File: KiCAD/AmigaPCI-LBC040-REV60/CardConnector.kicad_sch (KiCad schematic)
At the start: 42 parts, among them CN100 DIN41612_03x50, CN111 SPI, U111 ICE40HX4K-TQ144, U409F2 W25X20CLSN, X100 80MHz

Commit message: Add JLCPCB part numbers to KiCAD schematic.
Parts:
- C113, C114, C115, C116, C117, C135, C138: LCSC (none) -> C88724
- C122, C123, C124, C125, C126, C127, C128, C129, C130, C131, C133, C136, C137: LCSC (none) -> C14663
- C132, C134: LCSC (none) -> C96446
- CN111: LCSC (none) -> C37208
- R106, R107: LCSC (none) -> C25804
- R108, R109: LCSC (none) -> C22775
- R112, R113, R114, R115, R116, R117, R118, R119, R120: LCSC (none) -> C23345
- U111: LCSC (none) -> C1521989
- U409F2: LCSC (none) -> C34591
- X100: LCSC (none) -> C17234777

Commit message: Change JLCPCB part number for 80MHz oscillator.
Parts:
- X100: LCSC C17234777 -> C557215
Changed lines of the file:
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@@
 			)
 		)
-		(property "LCSC" "C17234777"
+		(property "LCSC" "C557215"
 			(at 358.14 157.48 0)
 			(effects

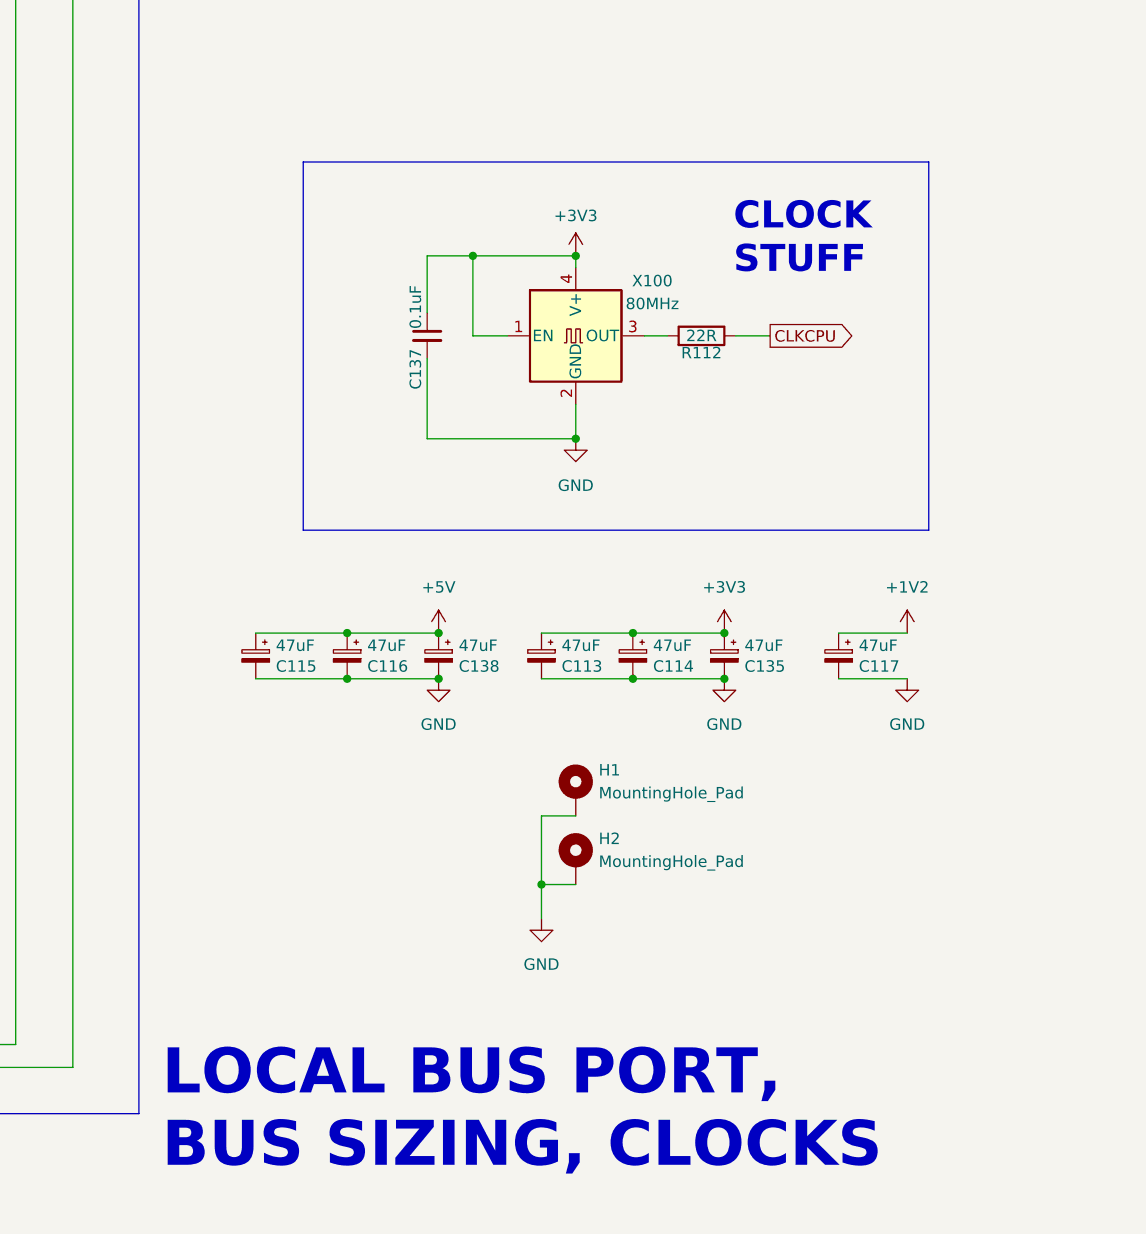
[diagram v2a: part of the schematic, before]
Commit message: Add part number for DIN41612 connector.
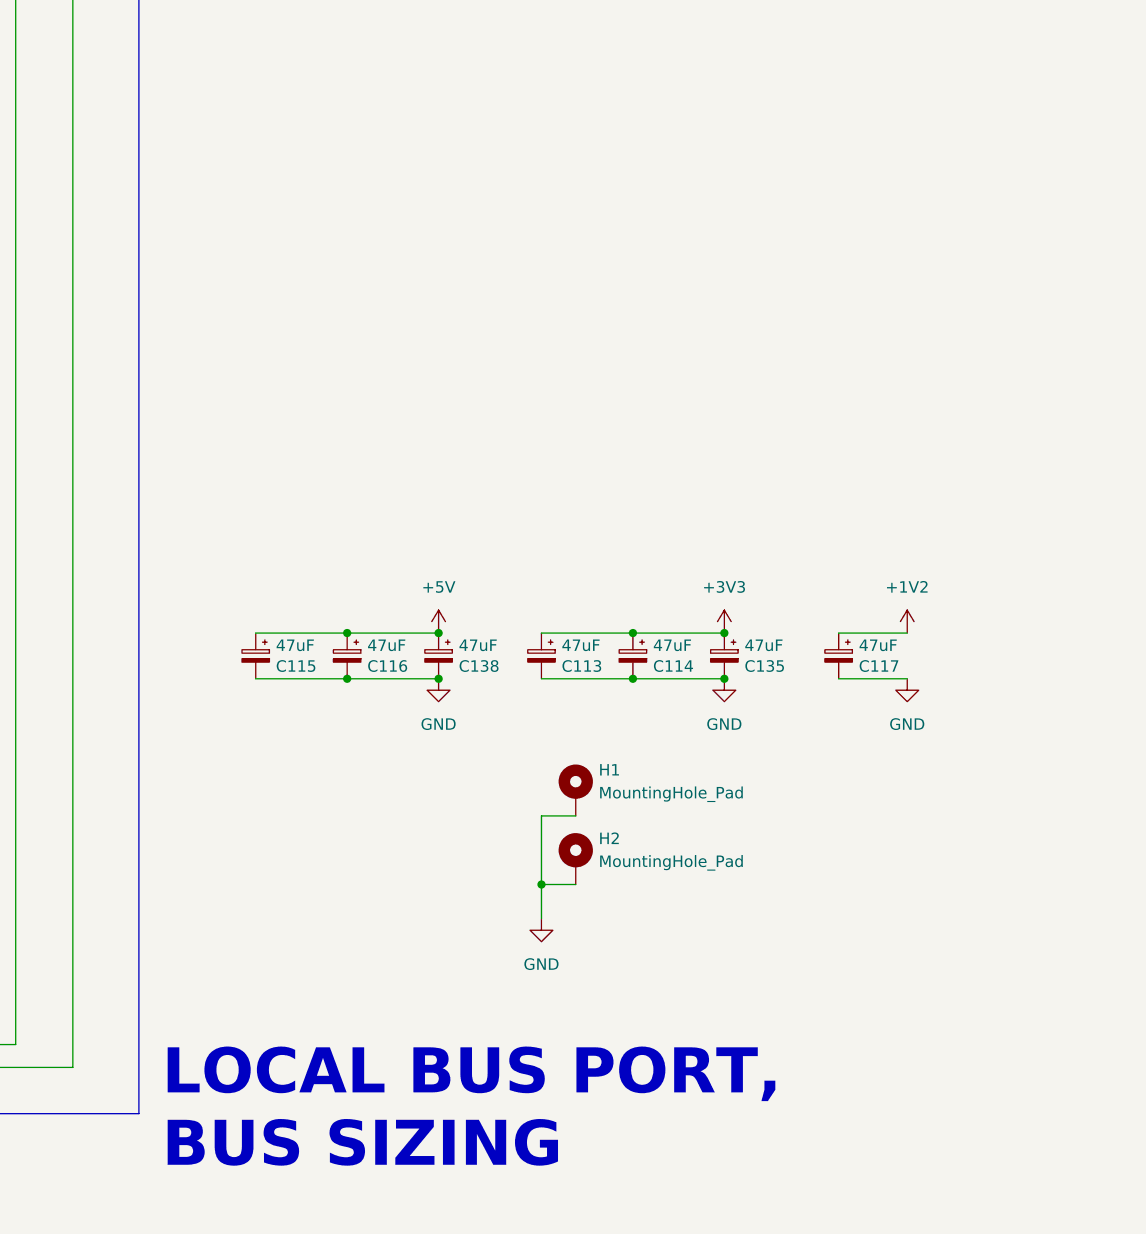
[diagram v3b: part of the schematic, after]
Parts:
- removed C137: 0.1uF, Capacitor_SMD:C_0603_1608Metric, symbol Device:C_Small
- removed R112: 22R, Resistor_SMD:R_0603_1608Metric, symbol Device:R
- removed X100: 80MHz, Oscillator:Oscillator_SMD_ECS_2520MV-xxx-xx-4Pin_2.5x2.0mm, symbol Oscillator:XO32
- CN100: LCSC (none) -> C3654550
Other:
- note added: "LOCAL BUS PORT, BUS SIZING"
- note removed: "CLOCK STUFF"
- note removed: "LOCAL BUS PORT, BUS SIZING, CLOCKS"
